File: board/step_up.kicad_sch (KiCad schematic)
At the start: 12 parts, among them U1 TLV61220

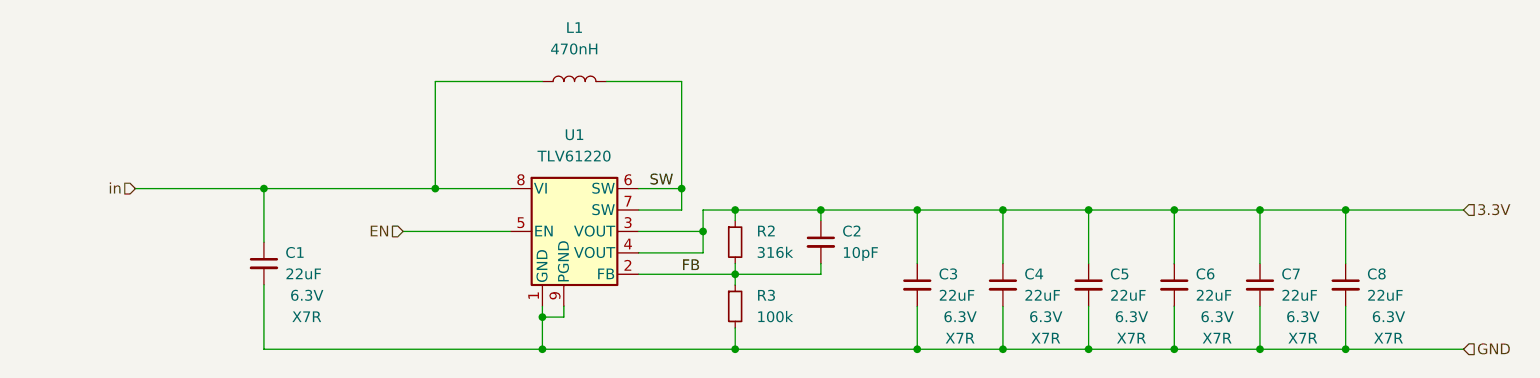
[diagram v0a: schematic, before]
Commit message: corrected U1 part number
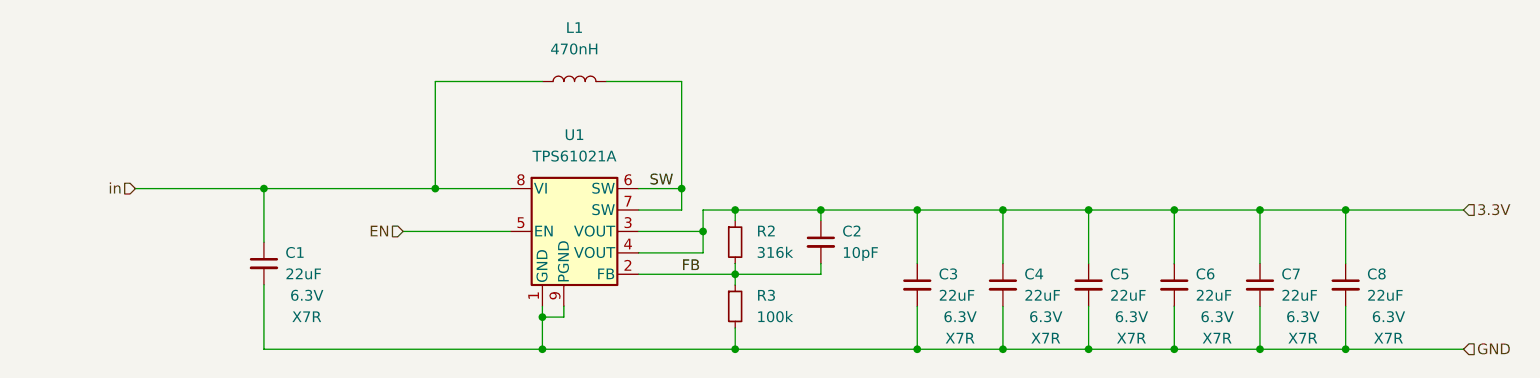
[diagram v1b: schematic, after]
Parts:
- U1: value TLV61220 -> TPS61021A; Digi-Key_PN (none) -> 296-TPS61021ADSGRCT-ND; MPN (none) -> TPS61021ADSGR
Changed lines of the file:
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@@
     (in_bom yes) (on_board yes) (fields_autoplaced)
     (property "Reference" "U1" (id 0) (at 138.43 102.87 0))
-    (property "Value" "TLV61220" (id 1) (at 138.43 105.41 0))
+    (property "Value" "TPS61021A" (id 1) (at 138.43 105.41 0))
     (property "Footprint" "Package_SON:WSON-8-1EP_2x2mm_P0.5mm_EP0.9x1.6mm" (id 2) (at 139.7 120.65 0)
       (effects (font (size 1.27 1.27) italic) (justify left) hide)
     )
-    (property "Datasheet" "https://www.ti.com/lit/ds/symlink/tlv61220.pdf" (id 3) (at 143.51 124.46 0)
+    (property "Datasheet" "https://www.ti.com/lit/ds/symlink/tps61021a.pdf?HQS=dis-dk-null-digikeymode-dsf-pf-null-wwe&ts=1678288703752&ref_url=https%253A%252F%252Fwww.ti.com%252Fgeneral%252Fdocs%252Fsuppproductinfo.tsp%253FdistId%253D10%2526gotoUrl%253Dhttps%253A%252F%252Fwww.ti.com%252Flit%252Fgpn%252Ftps61021a" (id 3) (at 143.51 124.46 0)
       (effects (font (size 1.27 1.27)) hide)
     )
+    (property "MPN" "TPS61021ADSGR" (id 4) (at 138.43 114.3 0)
+      (effects (font (size 1.27 1.27)) hide)
+    )
+    (property "Digi-Key_PN" "296-TPS61021ADSGRCT-ND" (id 5) (at 138.43 114.3 0)
+      (effects (font (size 1.27 1.27)) hide)
+    )

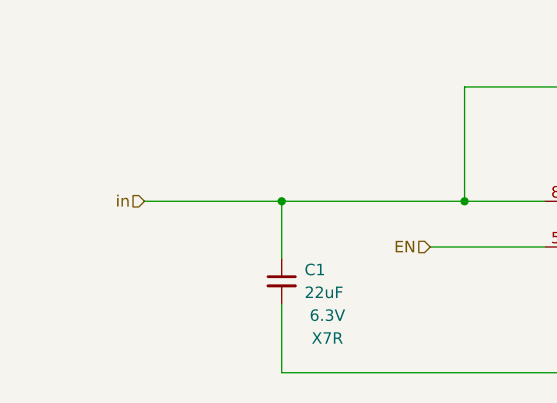
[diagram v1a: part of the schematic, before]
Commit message: added decoupling caps
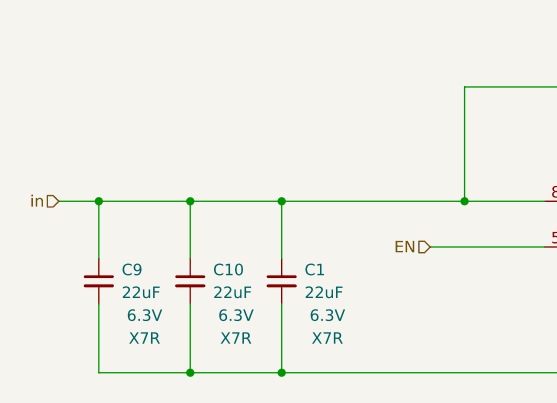
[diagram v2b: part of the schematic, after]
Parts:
- added C10, C9: 22uF, Capacitor_SMD:C_1206_3216Metric, symbol Device:C_Small
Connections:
- net GND: now also C10.2, C9.2
- net in: now also C10.1, C9.1
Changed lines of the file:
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@@
   (junction (at 209.55 128.27) (diameter 0) (color 0 0 0 0)
   )
+  (junction (at 101.6 128.27) (diameter 0) (color 0 0 0 0)
+  )
   (junction (at 153.67 114.3) (diameter 0) (color 0 0 0 0)
   )
   (junction (at 134.62 128.27) (diameter 0) (color 0 0 0 0)
   )
+  (junction (at 91.44 128.27) (diameter 0) (color 0 0 0 0)
+  )
   (junction (at 199.39 111.76) (diameter 0) (color 0 0 0 0)
   )
   (junction (at 157.48 111.76) (diameter 0) (color 0 0 0 0)
   )
+  (junction (at 91.44 109.22) (diameter 0) (color 0 0 0 0)
+  )
   (junction (at 134.62 124.46) (diameter 0) (color 0 0 0 0)
   )
@@
   (junction (at 121.92 109.22) (diameter 0) (color 0 0 0 0)
   )
+  (junction (at 81.28 109.22) (diameter 0) (color 0 0 0 0)
+  )
   (junction (at 101.6 109.22) (diameter 0) (color 0 0 0 0)
   )
@@
     (stroke (width 0) (type default) (color 0 0 0 0))
   )
+  (wire (pts (xy 91.44 109.22) (xy 101.6 109.22))
+    (stroke (width 0) (type default) (color 0 0 0 0))
+  )
   (wire (pts (xy 189.23 111.76) (xy 199.39 111.76))
     (stroke (width 0) (type default) (color 0 0 0 0))
@@
     (stroke (width 0) (type default) (color 0 0 0 0))
   )
+  (wire (pts (xy 91.44 109.22) (xy 91.44 115.57))
+    (stroke (width 0) (type default) (color 0 0 0 0))
+  )
   (wire (pts (xy 157.48 125.73) (xy 157.48 128.27))
     (stroke (width 0) (type default) (color 0 0 0 0))
   )
+  (wire (pts (xy 81.28 109.22) (xy 81.28 115.57))
+    (stroke (width 0) (type default) (color 0 0 0 0))
+  )
   (wire (pts (xy 209.55 128.27) (xy 219.71 128.27))
     (stroke (width 0) (type default) (color 0 0 0 0))
@@
     (stroke (width 0) (type default) (color 0 0 0 0))
   )
+  (wire (pts (xy 81.28 120.65) (xy 81.28 128.27))
+    (stroke (width 0) (type default) (color 0 0 0 0))
+  )
   (wire (pts (xy 219.71 123.19) (xy 219.71 128.27))
     (stroke (width 0) (type default) (color 0 0 0 0))
@@
     (stroke (width 0) (type default) (color 0 0 0 0))
   )
+  (wire (pts (xy 91.44 128.27) (xy 101.6 128.27))
+    (stroke (width 0) (type default) (color 0 0 0 0))
+  )
   (wire (pts (xy 229.87 128.27) (xy 243.84 128.27))
     (stroke (width 0) (type default) (color 0 0 0 0))
@@
     (stroke (width 0) (type default) (color 0 0 0 0))
   )
+  (wire (pts (xy 81.28 109.22) (xy 91.44 109.22))
+    (stroke (width 0) (type default) (color 0 0 0 0))
+  )
+  (wire (pts (xy 81.28 128.27) (xy 91.44 128.27))
+    (stroke (width 0) (type default) (color 0 0 0 0))
+  )
   (wire (pts (xy 134.62 96.52) (xy 121.92 96.52))
     (stroke (width 0) (type default) (color 0 0 0 0))
   )
+  (wire (pts (xy 91.44 120.65) (xy 91.44 128.27))
+    (stroke (width 0) (type default) (color 0 0 0 0))
+  )
   (wire (pts (xy 157.48 119.38) (xy 167.64 119.38))
     (stroke (width 0) (type default) (color 0 0 0 0))
@@
     (stroke (width 0) (type default) (color 0 0 0 0))
   )
-  (wire (pts (xy 86.36 109.22) (xy 101.6 109.22))
+  (wire (pts (xy 76.835 109.22) (xy 81.28 109.22))
     (stroke (width 0) (type default) (color 0 0 0 0))
   )
@@
     (effects (font (size 1.27 1.27)) (justify left))
   )
-  (hierarchical_label "in" (shape input) (at 86.36 109.22 180)
+  (hierarchical_label "in" (shape input) (at 76.835 109.22 180)
     (effects (font (size 1.27 1.27)) (justify right))
   )
@@
       (effects (font (size 1.27 1.27)) hide)
     )
+    (pin "1")
+    (pin "2")
+  )
+  (symbol (lib_id "Device:C_Small") (at 81.28 118.11 0) (unit 1)
+    (in_bom yes) (on_board yes)
+    (property "Reference" "C9" (id 0) (at 83.82 116.8462 0)
+      (effects (font (size 1.27 1.27)) (justify left))
+    )
+    (property "Value" "22uF" (id 1) (at 83.82 119.38 0)
+      (effects (font (size 1.27 1.27)) (justify left))
+    )
+    (property "Footprint" "Capacitor_SMD:C_1206_3216Metric" (id 2) (at 81.28 118.11 0)
+      (effects (font (size 1.27 1.27)) hide)
+    )
+    (property "Datasheet" "~" (id 3) (at 81.28 118.11 0)
+      (effects (font (size 1.27 1.27)) hide)
+    )
+    (property "Voltage" "6.3V" (id 4) (at 86.36 121.92 0))
+    (property "Dielectric" "X7R" (id 5) (at 86.36 124.46 0))
     (pin "1")
     (pin "2")
@@
     (pin "1")
     (pin "2")
+  )
+  (symbol (lib_id "Device:C_Small") (at 91.44 118.11 0) (unit 1)
+    (in_bom yes) (on_board yes)
+    (property "Reference" "C10" (id 0) (at 93.98 116.8462 0)
+      (effects (font (size 1.27 1.27)) (justify left))
+    )
+    (property "Value" "22uF" (id 1) (at 93.98 119.38 0)
+      (effects (font (size 1.27 1.27)) (justify left))
+    )
+    (property "Footprint" "Capacitor_SMD:C_1206_3216Metric" (id 2) (at 91.44 118.11 0)
+      (effects (font (size 1.27 1.27)) hide)
+    )
+    (property "Datasheet" "~" (id 3) (at 91.44 118.11 0)
+      (effects (font (size 1.27 1.27)) hide)
+    )
+    (property "Voltage" "6.3V" (id 4) (at 96.52 121.92 0))
+    (property "Dielectric" "X7R" (id 5) (at 96.52 124.46 0))
+    (pin "1")
+    (pin "2")
